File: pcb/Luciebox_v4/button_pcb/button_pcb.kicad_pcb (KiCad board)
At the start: 2 copper layers, 78 x 100 mm, 23 parts, among them T1 terminal_8x1, T2 terminal_8x1, T3 terminal_8x1, T4 terminal_2x1, U1 8X8PADS

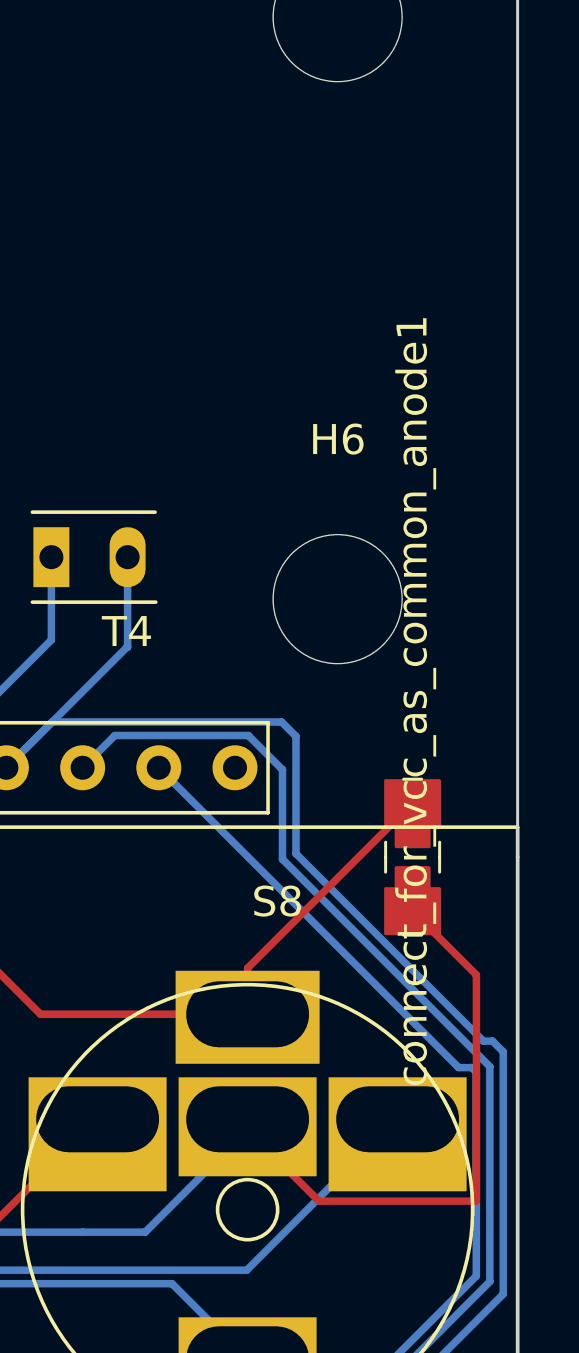
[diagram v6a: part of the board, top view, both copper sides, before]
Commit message: Add extra text and adjust artwork
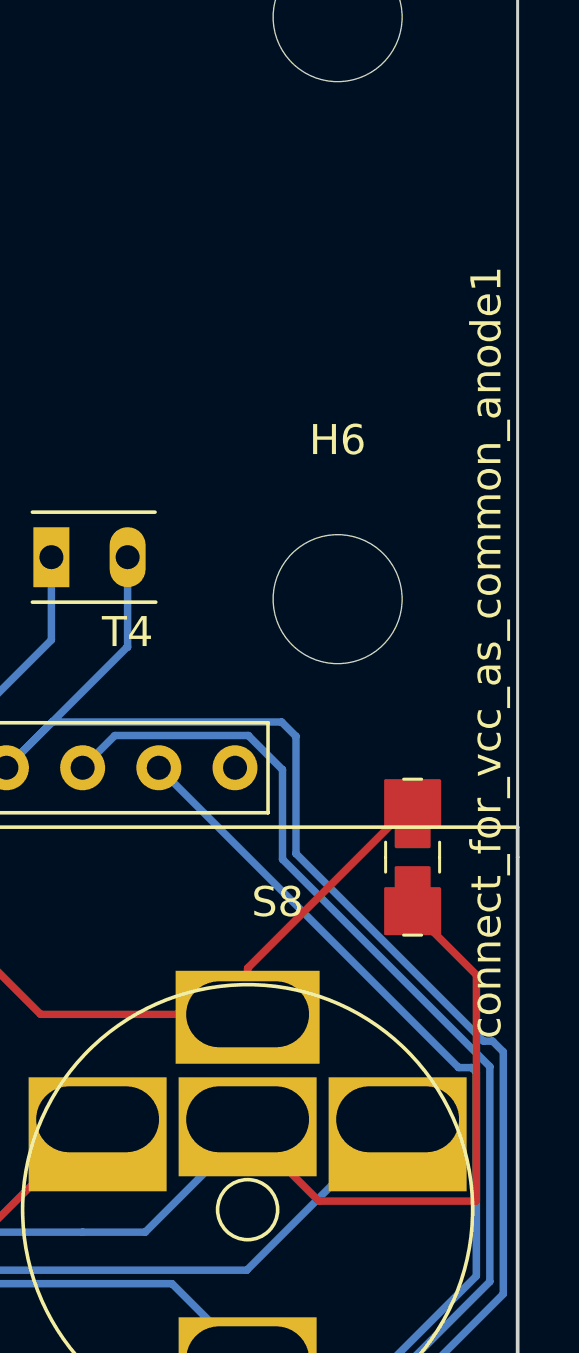
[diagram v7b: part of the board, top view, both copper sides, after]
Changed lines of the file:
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@@
     (property "Sheetname" "")
     (attr smd)
-    (fp_text reference "connect_for_vcc_as_common_anode1" (at 5.207 0 90) (layer "F.SilkS")
+    (fp_text reference "connect_for_vcc_as_common_anode1" (at 6.822 2.462 90) (layer "F.SilkS")
       (effects (font (size 1 1) (thickness 0.15)))
     )

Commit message: PCB v4 sent for production
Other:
- board text removed: "luciebox"
- board text removed: "luciebox.ameije.com"
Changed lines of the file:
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@@
       (outputformat 1)
       (mirror false)
-      (drillshape 1)
+      (drillshape 0)
       (scaleselection 1)
-      (outputdirectory "")
+      (outputdirectory "Fabrication/")
     )
   )
@@
     (effects (font (size 1 1) (thickness 0.15)) (justify left mirror))
   )
-  (gr_text "luciebox.ameije.com" (at 29.5 -49.6) (layer "F.SilkS")
-    (effects (font (size 1 1) (thickness 0.15)))
-  )
-  (gr_text "luciebox" (at 60.5 -51.6) (layer "F.SilkS")
-    (effects (font (size 4 4) (thickness 0.75)))
-  )
   (gr_text "lucie" (at 32.4 95) (layer "F.SilkS")
